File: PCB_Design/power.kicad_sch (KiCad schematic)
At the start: 18 parts, among them J4 Barrel_Jack, SW3 SW_DPST_x2, U1 NCP1117-3.3_SOT223, U4 NCP1117-3.3_SOT223, U6 NCP1117-5.0_SOT223

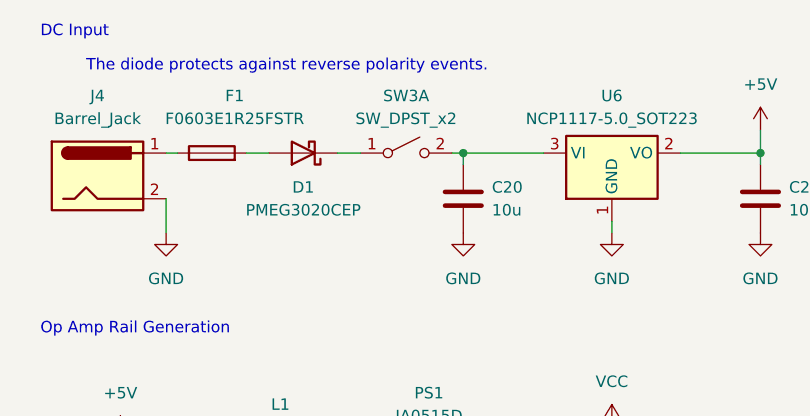
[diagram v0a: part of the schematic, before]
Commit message: KiCAD file update, completed PCB
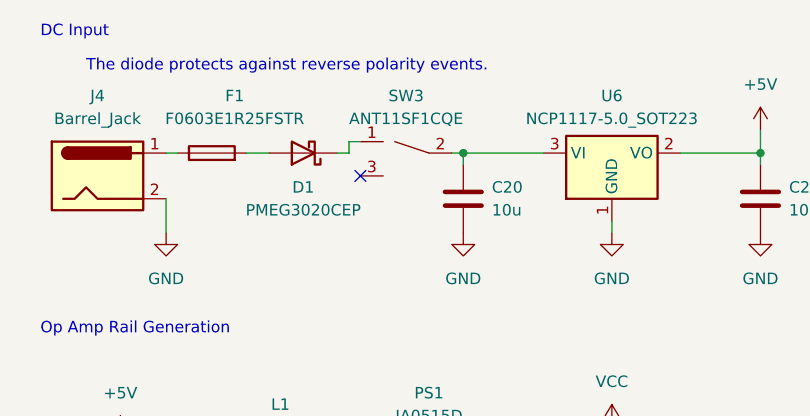
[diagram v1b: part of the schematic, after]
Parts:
- J4: footprint Connector_BarrelJack:BarrelJack_SwitchcraftConxall_RAPC10U_Horizontal -> Connector_BarrelJack:BarrelJack_GCT_DCJ200-10-A_Horizontal
- SW3: value SW_DPST_x2 -> ANT11SF1CQE; footprint Button_Switch_THT:SW_Push_2P1T_Toggle_CK_PVA1xxH1xxxxxxV2 -> ANT11SF1CQE:ANT11SF1CQE; symbol Switch:SW_DPST_x2 -> ANT11SF1CQE:ANT11SF1CQE
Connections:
- no-connect marks 0 -> 1
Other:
- moved on the sheet: SW3
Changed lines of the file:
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@@
   (junction (at 125.73 90.17) (diameter 0) (color 0 0 0 0)
   )
+  (no_connect (at 152.4 59.69))
   (wire (pts (xy 125.73 97.79) (xy 125.73 99.06))
     (stroke (width 0) (type default))
   )
+  (wire (pts (xy 151.13 57.15) (xy 149.86 57.15))
+    (stroke (width 0) (type default))
+  )
   (wire (pts (xy 180.34 97.79) (xy 180.34 99.06))
     (stroke (width 0) (type default))
@@
     (stroke (width 0) (type default))
   )
+  (wire (pts (xy 151.13 55.88) (xy 151.13 57.15))
+    (stroke (width 0) (type default))
+  )
   (wire (pts (xy 152.4 151.13) (xy 152.4 149.86))
     (stroke (width 0) (type default))
@@
     (stroke (width 0) (type default))
   )
-  (wire (pts (xy 149.86 57.15) (xy 152.4 57.15))
+  (wire (pts (xy 151.13 55.88) (xy 152.4 55.88))
     (stroke (width 0) (type default))
   )
@@
       (effects (font (size 1.27 1.27)))
     )
-    (property "Footprint" "Connector_BarrelJack:BarrelJack_SwitchcraftConxall_RAPC10U_Horizontal" (at 124.46 60.706 0)
+    (property "Footprint" "Connector_BarrelJack:BarrelJack_GCT_DCJ200-10-A_Horizontal" (at 124.46 60.706 0)
       (effects (font (size 1.27 1.27)) hide)
     )
@@
     )
   )
-  (symbol (lib_id "Switch:SW_DPST_x2") (at 157.48 57.15 0) (unit 1)
+  (symbol (lib_id "ANT11SF1CQE:ANT11SF1CQE") (at 153.67 55.88 0) (unit 1)
     (in_bom yes) (on_board yes) (dnp no) (fields_autoplaced)
     (property "Reference" "SW3" (at 157.48 50.8 0)
       (effects (font (size 1.27 1.27)))
     )
-    (property "Value" "SW_DPST_x2" (at 157.48 53.34 0)
-      (effects (font (size 1.27 1.27)))
-    )
-    (property "Footprint" "Button_Switch_THT:SW_Push_2P1T_Toggle_CK_PVA1xxH1xxxxxxV2" (at 157.48 57.15 0)
-      (effects (font (size 1.27 1.27)) hide)
-    )
-    (property "Datasheet" "~" (at 157.48 57.15 0)
-      (effects (font (size 1.27 1.27)) hide)
-    )
-    (pin "2")
-    (pin "4")
+    (property "Value" "ANT11SF1CQE" (at 157.48 53.34 0)
+      (effects (font (size 1.27 1.27)))
+    )
+    (property "Footprint" "ANT11SF1CQE:ANT11SF1CQE" (at 153.67 55.88 0)
+      (effects (font (size 1.27 1.27)) hide)
+    )
+    (property "Datasheet" "~" (at 153.67 55.88 0)
+      (effects (font (size 1.27 1.27)) hide)
+    )
+    (pin "2")
     (pin "1")
     (pin "3")

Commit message: Slight board updates - Added board PDFs and images
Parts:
- J4: symbol Connector:Barrel_Jack -> Connector:Barrel_Jack_Switch
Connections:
- net GND: now also J4.3
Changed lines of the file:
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@@
+    (stroke (width 0) (type default))
+  )
+  (wire (pts (xy 130.81 59.69) (xy 134.62 59.69))
     (stroke (width 0) (type default))
   )
@@
   )
   (wire (pts (xy 148.59 97.79) (xy 148.59 96.52))
+    (stroke (width 0) (type default))
+  )
+  (wire (pts (xy 134.62 59.69) (xy 134.62 60.96))
     (stroke (width 0) (type default))
   )
@@
     )
   )
-  (symbol (lib_id "Connector:Barrel_Jack") (at 123.19 59.69 0) (unit 1)
-    (in_bom yes) (on_board yes) (dnp no) (fields_autoplaced)
+  (symbol (lib_id "Connector:Barrel_Jack_Switch") (at 123.19 59.69 0) (unit 1)
+    (in_bom yes) (on_board yes) (dnp no)
     (property "Reference" "J4" (at 123.19 50.8 0)
       (effects (font (size 1.27 1.27)))
@@
     (pin "2")
     (pin "1")
+    (pin "3")
     (instances
       (project "picoAWG"
@@
         )
       )
+    )
+  )
+  (symbol (lib_id "power:GND") (at 134.62 60.96 0) (unit 1)
+    (in_bom yes) (on_board yes) (dnp no) (fields_autoplaced)
+    (property "Reference" "#PWR0247" (at 134.62 67.31 0)
+      (effects (font (size 1.27 1.27)) hide)
+    )
+    (property "Value" "GND" (at 134.62 66.04 0)
+      (effects (font (size 1.27 1.27)))
+    )
+    (property "Footprint" "" (at 134.62 60.96 0)
+      (effects (font (size 1.27 1.27)) hide)
+    )
+    (property "Datasheet" "" (at 134.62 60.96 0)
+      (effects (font (size 1.27 1.27)) hide)
+    )
+    (pin "1")
+    (instances
+      (project "picoAWG"
+        (path "/98622ba7-93bb-40c5-bd9c-32780137208f/45afd372-1c50-4efa-9ce4-01ad3c990303"
+          (reference "#PWR0247") (unit 1)
+        )
+      )

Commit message: Final KiCAD Files Submitted to JLC PCB
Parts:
- added D2: PMEG3020CEP, Diode_SMD:D_0603_1608Metric, symbol Device:D_Schottky
- C15: footprint Capacitor_SMD:C_0603_1608Metric -> Capacitor_THT:CP_Radial_D6.3mm_P2.50mm
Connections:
- net GND: now also SW3.3
- net at C20.1, SW3.2, U6.3 (VI): now also D2.1 (K)
- new net VBUS: D2.2 (A)
- no-connect marks 1 -> 0
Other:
- note removed: "The diode protects against reverse polarity events."
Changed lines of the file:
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@@
   (junction (at 138.43 97.79) (diameter 0) (color 0 0 0 0)
   )
+  (junction (at 167.64 57.15) (diameter 0) (color 0 0 0 0)
+  )
   (junction (at 125.73 97.79) (diameter 0) (color 0 0 0 0)
   )
@@
   (junction (at 125.73 90.17) (diameter 0) (color 0 0 0 0)
   )
-  (no_connect (at 152.4 59.69))
   (wire (pts (xy 125.73 97.79) (xy 125.73 99.06))
     (stroke (width 0) (type default))
@@
     (stroke (width 0) (type default))
   )
+  (wire (pts (xy 167.64 49.53) (xy 167.64 57.15))
+    (stroke (width 0) (type default))
+  )
   (wire (pts (xy 180.34 97.79) (xy 180.34 99.06))
     (stroke (width 0) (type default))
@@
     (stroke (width 0) (type default))
   )
+  (wire (pts (xy 167.64 39.37) (xy 167.64 41.91))
+    (stroke (width 0) (type default))
+  )
   (wire (pts (xy 196.85 57.15) (xy 196.85 58.42))
     (stroke (width 0) (type default))
@@
     (stroke (width 0) (type default))
   )
+  (wire (pts (xy 152.4 59.69) (xy 152.4 60.96))
+    (stroke (width 0) (type default))
+  )
   (wire (pts (xy 152.4 151.13) (xy 152.4 149.86))
     (stroke (width 0) (type default))
@@
     (stroke (width 0) (type default))
   )
+  (wire (pts (xy 167.64 57.15) (xy 172.72 57.15))
+    (stroke (width 0) (type default))
+  )
   (wire (pts (xy 138.43 97.79) (xy 148.59 97.79))
     (stroke (width 0) (type default))
   )
+  (wire (pts (xy 156.21 60.96) (xy 156.21 63.5))
+    (stroke (width 0) (type default))
+  )
   (wire (pts (xy 130.81 59.69) (xy 134.62 59.69))
     (stroke (width 0) (type default))
@@
     (stroke (width 0) (type default))
   )
-  (wire (pts (xy 163.83 57.15) (xy 172.72 57.15))
+  (wire (pts (xy 163.83 57.15) (xy 167.64 57.15))
     (stroke (width 0) (type default))
   )
@@
   )
   (wire (pts (xy 134.62 115.57) (xy 134.62 116.84))
+    (stroke (width 0) (type default))
+  )
+  (wire (pts (xy 152.4 60.96) (xy 156.21 60.96))
     (stroke (width 0) (type default))
   )
@@
     (effects (font (size 1.27 1.27)) (justify right bottom))
   )
-  (text "The diode protects against reverse polarity events."
-    (at 121.92 48.26 0)
-    (effects (font (size 1.27 1.27)) (justify left bottom))
-  )
   (text "Op Amp Rail Generation" (at 116.84 77.47 0)
     (effects (font (size 1.27 1.27)) (justify left bottom))
   )
+  (symbol (lib_id "Device:D_Schottky") (at 167.64 45.72 90) (unit 1)
+    (in_bom yes) (on_board yes) (dnp no)
+    (property "Reference" "D2" (at 177.8 44.45 90)
+      (effects (font (size 1.27 1.27)))
+    )
+    (property "Value" "PMEG3020CEP" (at 177.8 46.99 90)
+      (effects (font (size 1.27 1.27)))
+    )
+    (property "Footprint" "Diode_SMD:D_0603_1608Metric" (at 167.64 45.72 0)
+      (effects (font (size 1.27 1.27)) hide)
+    )
+    (property "Datasheet" "~" (at 167.64 45.72 0)
+      (effects (font (size 1.27 1.27)) hide)
+    )
+    (pin "2")
+    (pin "1")
+    (instances
+      (project "picoAWG"
+        (path "/98622ba7-93bb-40c5-bd9c-32780137208f/45afd372-1c50-4efa-9ce4-01ad3c990303"
+          (reference "D2") (unit 1)
+        )
+      )
+    )
+  )
   (symbol (lib_id "power:GND") (at 134.62 149.86 0) (unit 1)
     (in_bom yes) (on_board yes) (dnp no) (fields_autoplaced)
@@
         (path "/98622ba7-93bb-40c5-bd9c-32780137208f/45afd372-1c50-4efa-9ce4-01ad3c990303"
           (reference "#PWR018") (unit 1)
+        )
+      )
+    )
+  )
+  (symbol (lib_id "power:GND") (at 156.21 63.5 0) (unit 1)
+    (in_bom yes) (on_board yes) (dnp no) (fields_autoplaced)
+    (property "Reference" "#PWR0248" (at 156.21 69.85 0)
+      (effects (font (size 1.27 1.27)) hide)
+    )
+    (property "Value" "GND" (at 156.21 68.58 0)
+      (effects (font (size 1.27 1.27)))
+    )
+    (property "Footprint" "" (at 156.21 63.5 0)
+      (effects (font (size 1.27 1.27)) hide)
+    )
+    (property "Datasheet" "" (at 156.21 63.5 0)
+      (effects (font (size 1.27 1.27)) hide)
+    )
+    (pin "1")
+    (instances
+      (project "picoAWG"
+        (path "/98622ba7-93bb-40c5-bd9c-32780137208f/45afd372-1c50-4efa-9ce4-01ad3c990303"
+          (reference "#PWR0248") (unit 1)
         )
       )
@@
       (effects (font (size 1.27 1.27)) (justify left))
     )
-    (property "Footprint" "Capacitor_SMD:C_0603_1608Metric" (at 126.6952 97.79 0)
+    (property "Footprint" "Capacitor_THT:CP_Radial_D6.3mm_P2.50mm" (at 126.6952 97.79 0)
       (effects (font (size 1.27 1.27)) hide)
     )
@@
         )
       )
+    )
+  )
+  (symbol (lib_id "power:VBUS") (at 167.64 39.37 0) (unit 1)
+    (in_bom yes) (on_board yes) (dnp no) (fields_autoplaced)
+    (property "Reference" "#PWR0250" (at 167.64 43.18 0)
+      (effects (font (size 1.27 1.27)) hide)
+    )
+    (property "Value" "VBUS" (at 167.64 34.29 0)
+      (effects (font (size 1.27 1.27)))
+    )
+    (property "Footprint" "" (at 167.64 39.37 0)
+      (effects (font (size 1.27 1.27)) hide)
+    )
+    (property "Datasheet" "" (at 167.64 39.37 0)
+      (effects (font (size 1.27 1.27)) hide)
+    )
+    (pin "1")
+    (instances
+      (project "picoAWG"
+        (path "/98622ba7-93bb-40c5-bd9c-32780137208f/45afd372-1c50-4efa-9ce4-01ad3c990303"
+          (reference "#PWR0250") (unit 1)
+        )
+      )

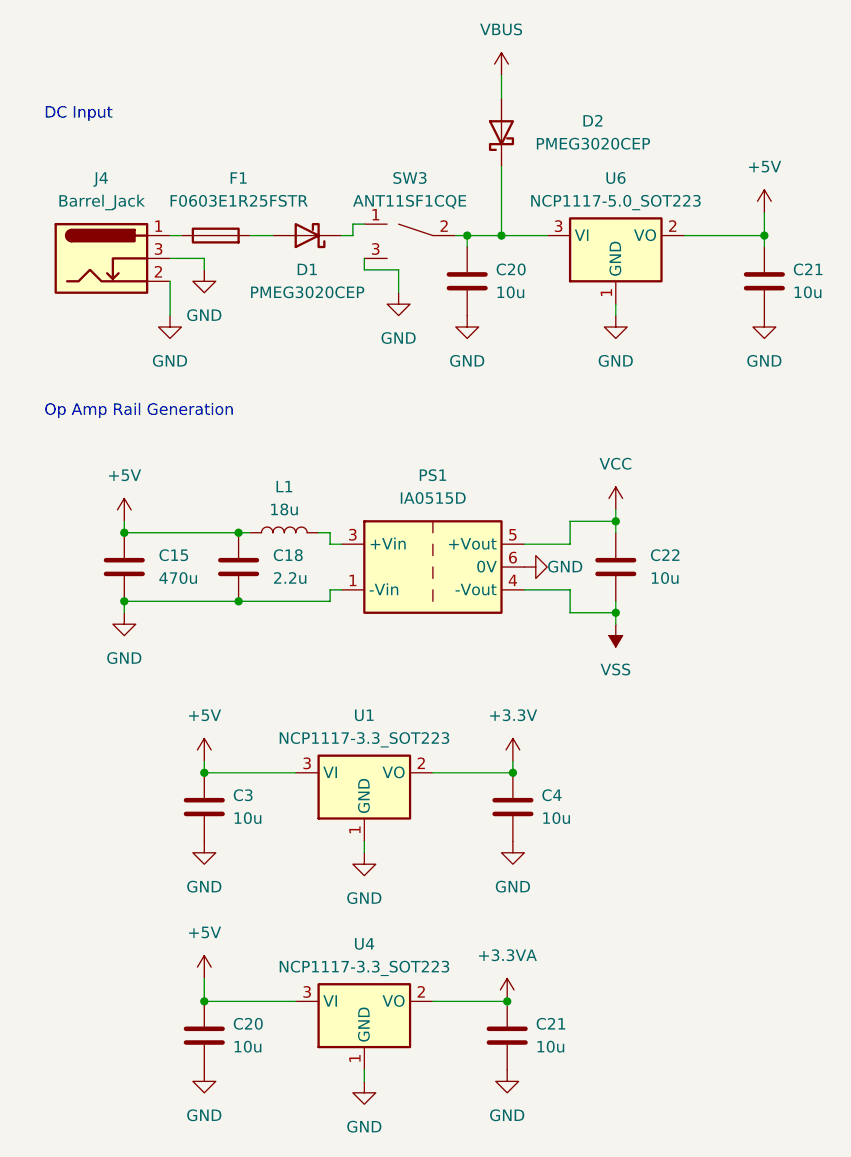
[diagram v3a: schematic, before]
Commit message: Update KiCAD files to KiCAD 8.0
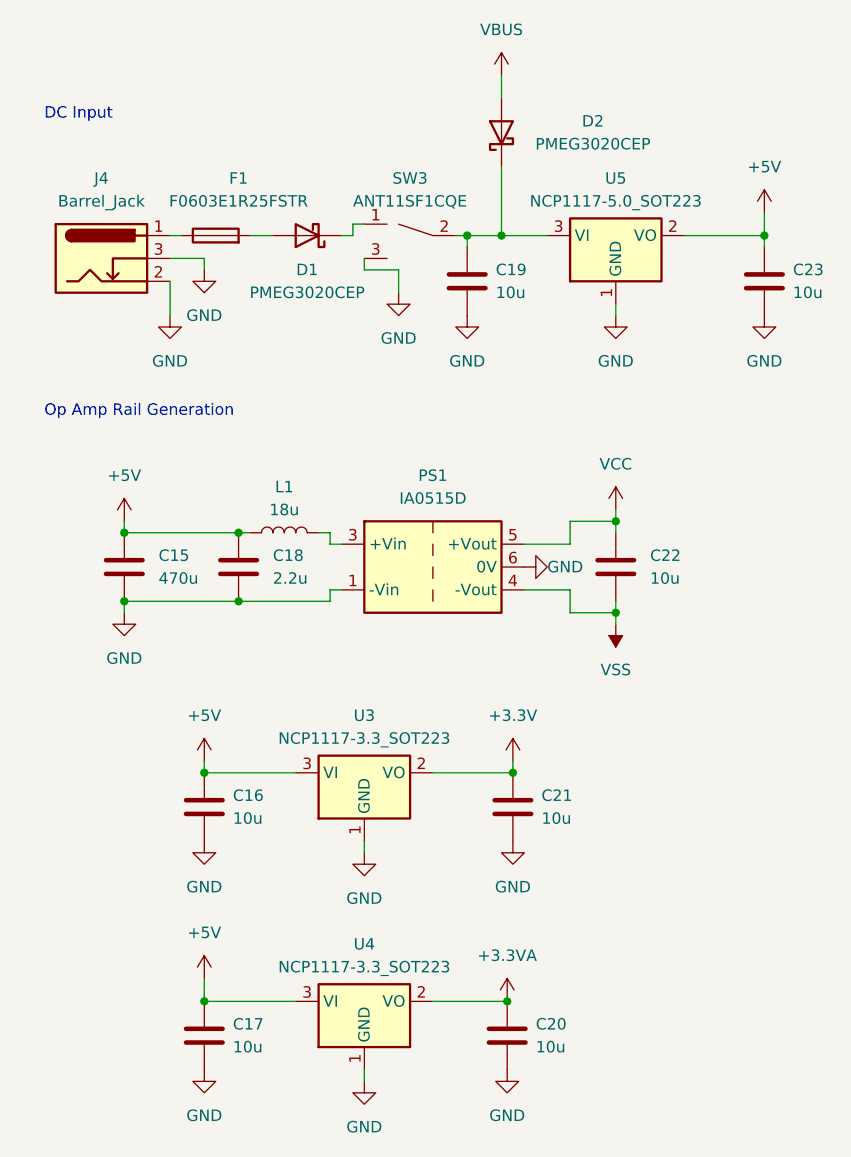
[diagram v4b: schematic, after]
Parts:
- renumbered C3 to C16, C20 to C17, C20 to C19, C21 to C20, C4 to C21, C21 to C23, U1 to U3, U6 to U5
